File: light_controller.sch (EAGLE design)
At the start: 105 parts, among them U1 DAC5578SPW, U2 MPM3620GQV-P, U3 RCD-24-0.70, U4 PHOTONH, U5 ISO1540DR

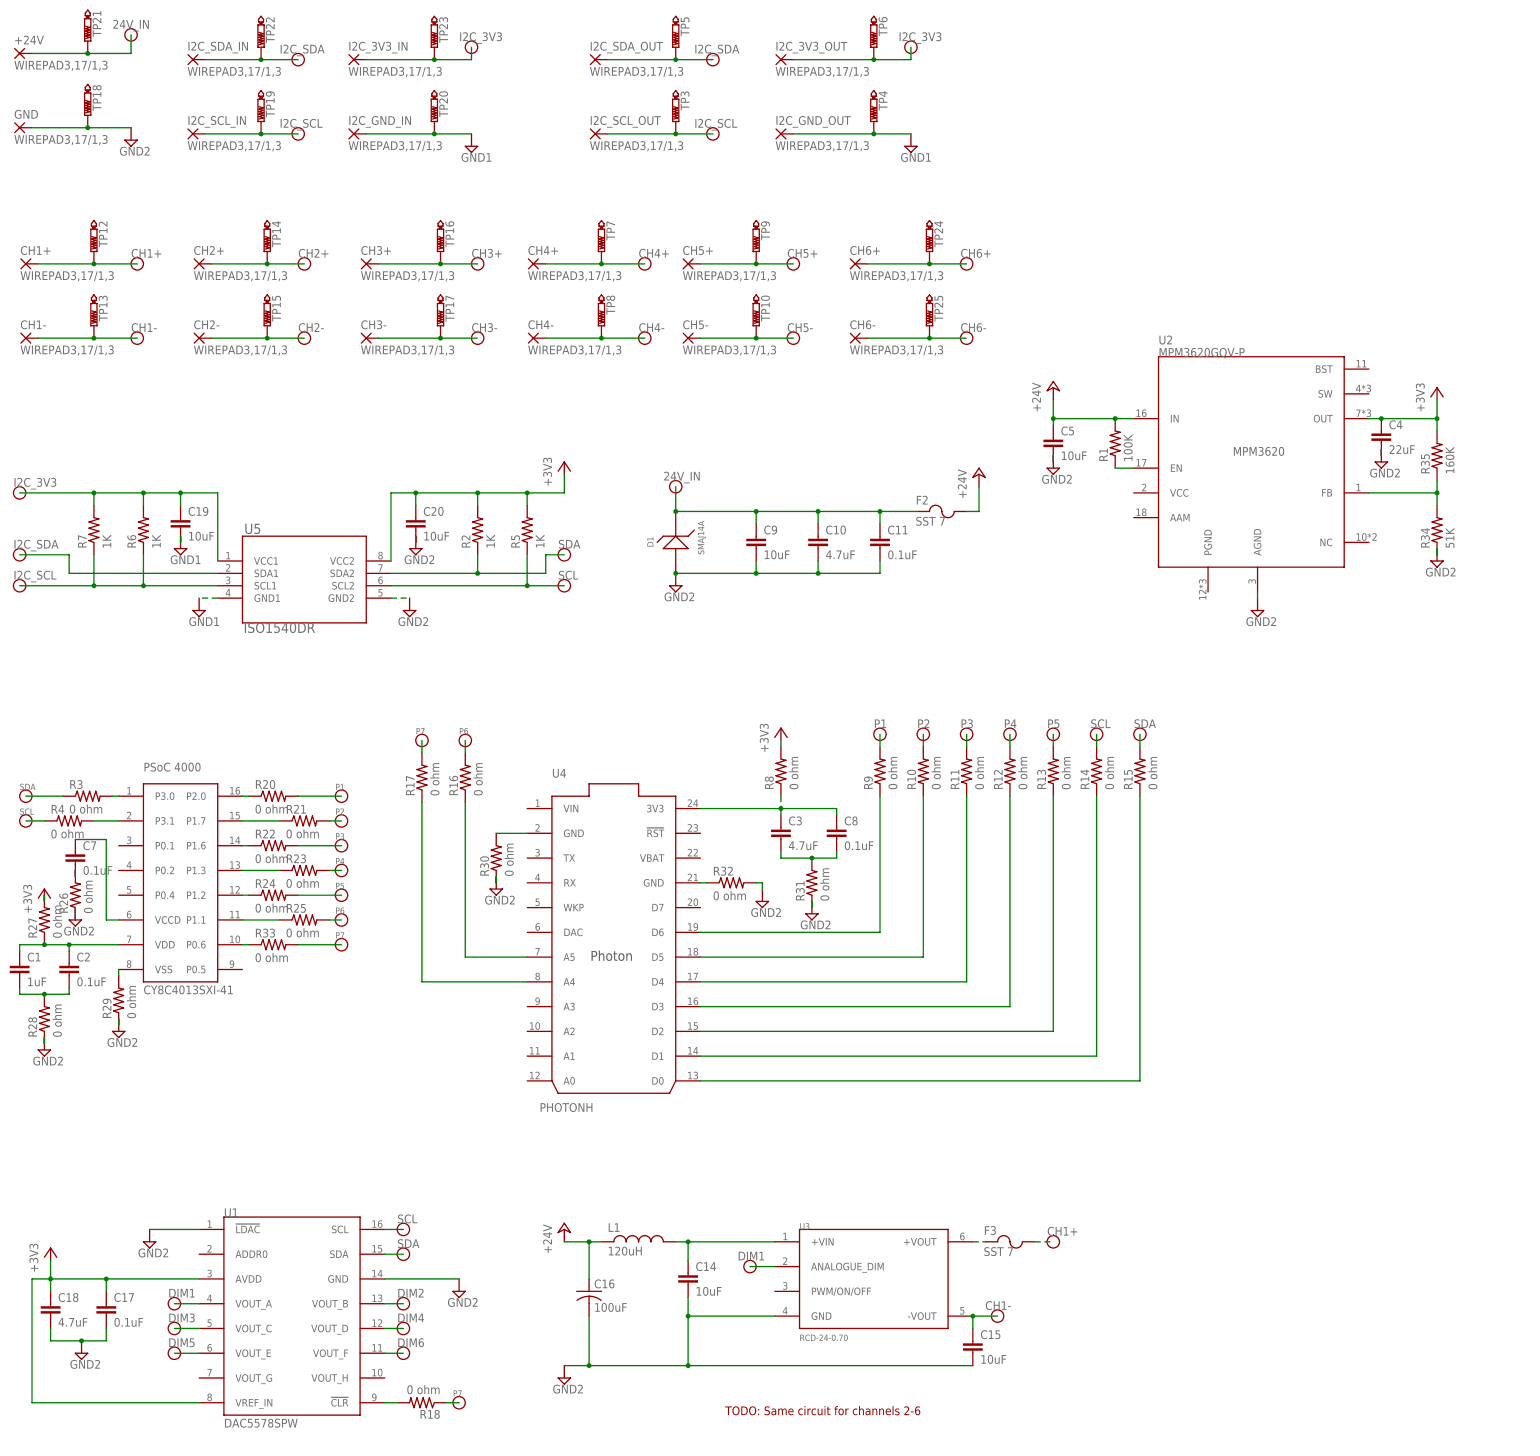
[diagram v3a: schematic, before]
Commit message: added x2y cap for 24v conditioning and testpoints for self-contined module testing
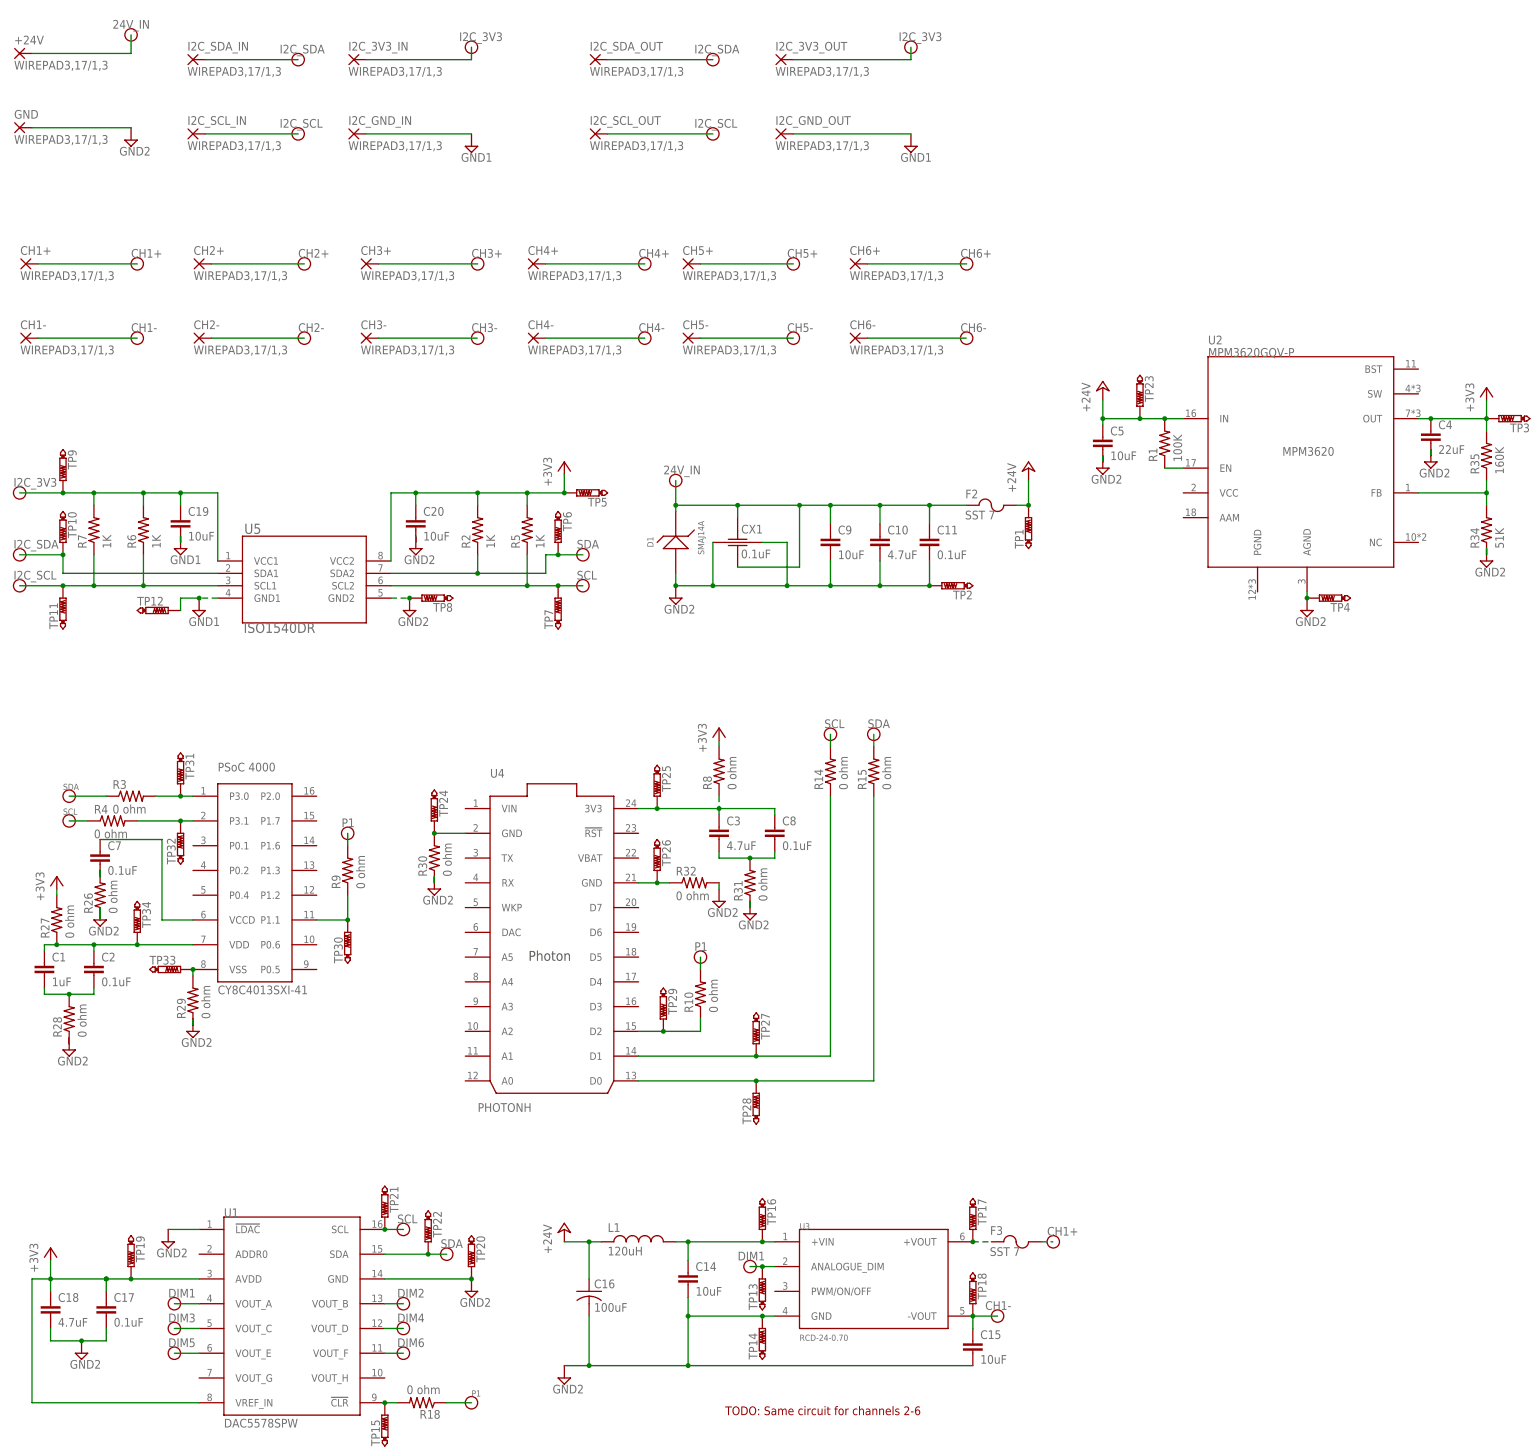
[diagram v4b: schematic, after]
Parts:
- removed R11, R12, R13, R16, R17, R20, R21, R22, R23, R24, R25, R33: 0 ohm, openag-resistors:0OHM-ERJ-3GEY0R00V
- added CX1: 0.1uF, openag-capacitors:0.1UF-X2Y-CX1206MKX7R9BB104
- added TP1, TP11, TP2, TP26, TP27, TP28, TP29, TP30, TP31, TP32, TP33, TP34: PTR1B2,54, openag-testpoints:PTR1B2,54
- TP10, TP12, TP13, TP14, TP15, TP16, TP17, TP18, TP19, TP20, TP21, TP22, TP23, TP24, TP25, TP3, TP4, TP5, TP6, TP7, TP8, TP9: device testpad:PTR1B2,54 -> openag-testpoints:PTR1B2,54
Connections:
- removed net N$10: R21.1, U$2.P1.7
- removed net N$11: R22.1, U$2.P1.6
- removed net N$12: R23.1, U$2.P1.3
- removed net N$13: R24.1, U$2.P1.2
- removed net N$14: R25.1, U$2.P1.1
- removed net N$21: R13.1, U4.D2
- removed net N$24: R9.1, U4.D6
- removed net N$25: R10.1, U4.D5
- removed net N$26: R11.1, U4.D4
- removed net N$27: R12.1, U4.D3
- removed net N$31: R33.1, U$2.P0.6
- removed net N$6: R17.1, U4.A4
- removed net P2: R10.2, R21.2
- removed net P3: R11.2, R22.2
- removed net P4: R12.2, R23.2
- removed net P5: R13.2, R24.2
- removed net P6: R16.2, R25.2
- removed net P7: R17.2, R18.1, R33.2
- net +24V: now also TP1.TP, TP23.TP
- net +3V3: now also TP19.TP, TP3.TP, TP5.TP
- net 24V_IN: now also CX1.11, CX1.22; no longer TP21.TP
- net CH1+: no longer TP12.TP
- net CH1-: now also TP18.TP; no longer TP13.TP
- net CH2+: no longer TP14.TP
- net CH2-: no longer TP15.TP
- net CH3+: no longer TP16.TP
- net CH3-: no longer TP17.TP
- net CH4+: no longer TP7.TP
- net CH4-: no longer TP8.TP
- net CH5+: no longer TP9.TP
- net CH5-: no longer TP10.TP
- net CH6+: no longer TP24.TP
- net CH6-: no longer TP25.TP
- net DIM1: now also TP13.TP
- net GND1: now also TP12.TP; no longer TP20.TP, TP4.TP
- net GND2: now also CX1.33, CX1.44, TP14.TP, TP2.TP, TP20.TP, TP4.TP, TP8.TP; no longer TP18.TP
- net I2C_3V3: now also TP9.TP; no longer TP23.TP, TP6.TP
- net I2C_SCL: now also TP11.TP; no longer TP19.TP, TP3.TP
- net I2C_SDA: now also TP10.TP; no longer TP22.TP, TP5.TP
- net N$1: now also TP31.TP
- net N$16: now also TP34.TP
- net N$18: now also TP33.TP
- net N$19: now also TP24.TP
- net N$2: now also TP32.TP
- net N$22: now also TP27.TP
- net N$23: now also TP25.TP
- net N$28: now also TP28.TP
- net N$3: now also TP16.TP
- net N$30: now also TP26.TP
- net N$4: now also R9.1, TP30.TP, U$2.P1.1; no longer R16.1, U4.A5
- net N$5: now also TP17.TP
- net N$7: now also R10.1, TP29.TP, U4.D2; no longer R20.1, U$2.P2.0
- net N$8: now also TP15.TP
- net P1: now also R10.2, R18.1; no longer R20.2
- net SCL: now also TP21.TP, TP7.TP
- net SDA: now also TP22.TP, TP6.TP
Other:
- moved on the sheet: C1, C10, C11, C2, C3, C4, C5, C7, C8, C9, F2, F3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

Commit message: routed current regulators and 3.3v sync regulators, added rs485 to ttl transceiver
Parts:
- removed I2C_3V3_IN, I2C_3V3_OUT, I2C_GND_IN, I2C_GND_OUT, I2C_SCL_IN, I2C_SCL_OUT, I2C_SDA_IN, I2C_SDA_OUT: WIREPAD3,17/1,3, wirepad:WIREPAD3,17/1,3
- removed R26, R28, R29, R30: 0 ohm, openag-resistors:0OHM-ERJ-3GEY0R00V
- removed TP10, TP11, TP12, TP15, TP19, TP20, TP21, TP22, TP23, TP24, TP25, TP26, TP27, TP28, TP29, TP30, TP31, TP32, TP33, TP34, TP4, TP9: PTR1B2,54, openag-testpoints:PTR1B2,54
- added 3V3_IN, 3V3_OUT, 5V_IN, 5V_OUT, GND_IN, GND_OUT, RX_IN, RX_OUT, SCL_IN, SCL_OUT, SDA_IN, SDA_OUT, TX_IN, TX_OUT, _GND_IN, _GND_OUT: (no value), openag-wirepads:3,17/1,3
- added C12, C21, C22, C24, C25, C27, C28, C30, C31, C6: 10uF, openag-capacitors:10UF-CL31B106KBHNNNE
- added C13, C23, C26, C29, C32: 100uF, openag-capacitors:100UF-EEE-1HA101UP
- added C33: 330pF, openag-capacitors:330PF-CC1206KRX7R9BB331
- added F1, F4, F5, F6, F7: SST 7, openag-fuses:SST_7
- added L2, L3, L4, L5, L6: 120uH, openag-inductors:120UH-74404064121
- added R11: 6.34 ohm, openag-resistors:6.3OHM-RC0805FR-076R34L
- added R12: 16.5K, openag-resistors:16.5K-311-16.5KHRCT-ND
- added TP35, TP36, TP37, TP38, TP39, TP40, TP41, TP42, TP43, TP44, TP45, TP46, TP47, TP48, TP49, TP50, TP51, TP52, TP53, TP54, TP55, TP56, TP57, TP58, TP59: PTR1B2,54, openag-testpoints:PTR1B2,54
- added U10, U6, U7, U8, U9: RCD-24-0.70, openag-regulators:RCD-24-0.70
- added U11: MAX3485CSA+T, openag-transceivers:MAX3485CSA+T
- +24V, CH1+, CH1-, CH2+, CH2-, CH3+, CH3-, CH4+, CH4-, CH5+, CH5-, CH6+, CH6-, GND: value WIREPAD3,17/1,3 -> (none); device wirepad:WIREPAD3,17/1,3 -> openag-wirepads:3,17/1,3
- R1: value 100K -> 200K; device openag-resistors:100K-RC0603FR-07100KL -> openag-resistors:200K-RC0603JR-07200KL
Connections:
- new net 485_5V: 5V_IN.P, 5V_OUT.P
- new net 485_A: U11.A
- new net 485_B: U11.B
- new net 485_RX: RX_IN.P, RX_OUT.P
- new net 485_TX: TX_IN.P, TX_OUT.P
- new net N$10: C21.1, L3.2, TP42.TP, U7.+VIN
- new net N$11: F4.1, TP43.TP, U7.+VOUT
- new net N$12: C24.1, L4.2, TP47.TP, U8.+VIN
- new net N$13: F5.1, TP48.TP, U8.+VOUT
- new net N$14: C27.1, L5.2, TP52.TP, U9.+VIN
- new net N$21: F6.1, TP53.TP, U9.+VOUT
- new net N$24: C30.1, L6.2, TP57.TP, U10.+VIN
- new net N$25: F7.1, TP58.TP, U10.+VOUT
- new net N$26: U11.DE
- new net N$27: U11.RO
- new net N$31: U11.!RE!
- new net N$6: C6.1, L2.2, TP37.TP, U6.+VIN
- new net N$9: F1.1, TP38.TP, U6.+VOUT
- net +24V: now also C10.1, C11.1, C13.1(+), C23.1(+), C26.1(+), C29.1(+), C32.1(+), C9.1, CX1.11, CX1.22, D1.P$2, L2.1, L3.1, L4.1, L5.1, L6.1; no longer TP23.TP
- net +3V3: now also U11.VCC; no longer TP19.TP
- net 24V_IN: no longer C10.1, C11.1, C9.1, CX1.11, CX1.22, D1.P$2
- net CH2+: now also F1.2
- net CH2-: now also C12.1, TP39.TP, U6.-VOUT
- net CH3+: now also F4.2
- net CH3-: now also C22.1, TP44.TP, U7.-VOUT
- net CH4+: now also F5.2
- net CH4-: now also C25.1, TP49.TP, U8.-VOUT
- net CH5+: now also F6.2
- net CH5-: now also C28.1, TP54.TP, U9.-VOUT
- net CH6+: now also F7.2
- net CH6-: now also C31.1, TP59.TP, U10.-VOUT
- net DIM2: now also TP35.TP, U6.ANALOGUE_DIM
- net DIM3: now also TP40.TP, U7.ANALOGUE_DIM
- net DIM4: now also TP45.TP, U8.ANALOGUE_DIM
- net DIM5: now also TP50.TP, U9.ANALOGUE_DIM
- net DIM6: now also TP55.TP, U10.ANALOGUE_DIM
- net GND1: now also GND_IN.P, GND_OUT.P, U11.GND, _GND_IN.P, _GND_OUT.P; no longer I2C_GND_IN.P, I2C_GND_OUT.P, TP12.TP
- net GND2: now also C1.2, C12.2, C13.2(-), C2.2, C21.2, C22.2, C23.2(-), C24.2, C25.2, C26.2(-), C27.2, C28.2, C29.2(-), C30.2, C31.2, C32.2(-), C33.2, C6.2, C7.2, R12.1, TP36.TP, TP41.TP, TP46.TP, TP51.TP, TP56.TP, U$2.VSS, U10.GND, U2.PGND, U6.GND, U7.GND, U8.GND, U9.GND; no longer R26.1, R28.1, R29.1, R30.1, TP20.TP, TP4.TP
- net I2C_3V3: now also 3V3_IN.P, 3V3_OUT.P; no longer I2C_3V3_IN.P, I2C_3V3_OUT.P, TP9.TP
- net I2C_SCL: now also SCL_IN.P, SCL_OUT.P; no longer I2C_SCL_IN.P, I2C_SCL_OUT.P, R6.1, TP11.TP
- net I2C_SDA: now also R6.1, SDA_IN.P, SDA_OUT.P; no longer I2C_SDA_IN.P, I2C_SDA_OUT.P, TP10.TP
- net N$1: no longer TP31.TP
- net N$15: now also R11.2, U2.SW; no longer C7.2, R26.2
- net N$16: no longer TP34.TP
- net N$17: now also C33.1, R11.1; no longer C1.2, C2.2, R28.2
- net N$18: now also R12.2, U2.AAM; no longer R29.2, TP33.TP, U$2.VSS
- net N$19: now also U11.DI; no longer R30.2, TP24.TP, U4.GND@2
- net N$2: no longer TP32.TP
- net N$22: no longer TP27.TP
- net N$23: no longer TP25.TP
- net N$28: no longer TP28.TP
- net N$30: now also U4.GND@2; no longer TP26.TP
- net N$4: no longer TP30.TP
- net N$7: no longer TP29.TP
- net N$8: no longer TP15.TP
- net SCL: no longer TP21.TP
- net SDA: no longer TP22.TP
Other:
- note added: "RS485 Input"
- note added: "RS485 Output"
- note added: "changelog - shifted from 12V power to 24V - shifted from i2c as external comm to rs485"
- note removed: "TODO: Same circuit for channels 2-6"
- moved on the sheet: C10, C11, C4, C5, C7, C9, CX1, D1, F2, R1, R34, R35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
